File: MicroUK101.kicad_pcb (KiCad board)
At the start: 2 copper layers, 99.7 x 92.5 mm, 31 parts, among them CON1 BARREL_JACK, J1 DB9, P1 CONN_02X02, P2 CONN_01X04, P3 CONN_02X01, P4 CONN_02X01, SW1 SW_PUSH, SW2 Switch_DPST, U1 6502, U10 74LS00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

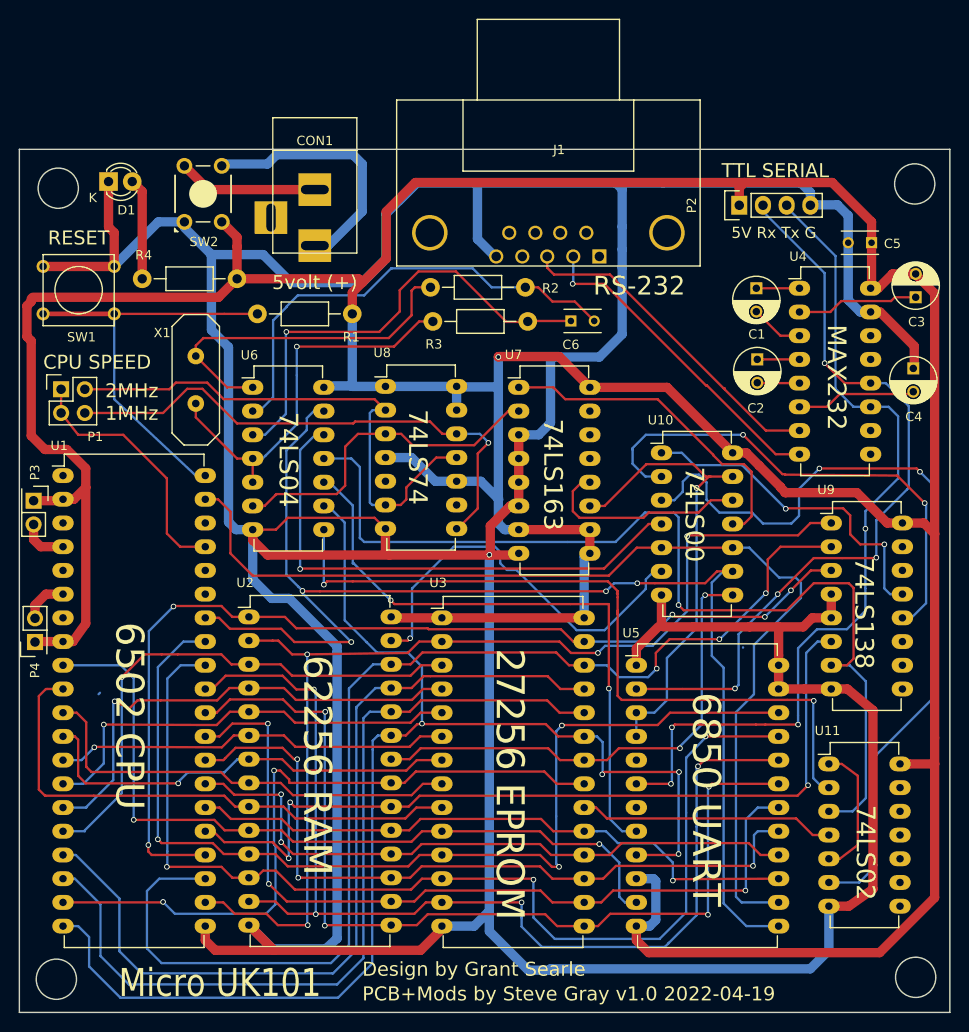
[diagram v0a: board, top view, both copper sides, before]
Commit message: Release 1.02
Fix Tx and Rx lines to RS-232. Ran DRC and fixed a bunch of small track
errors. Updated silkscreen, created new gerbers.
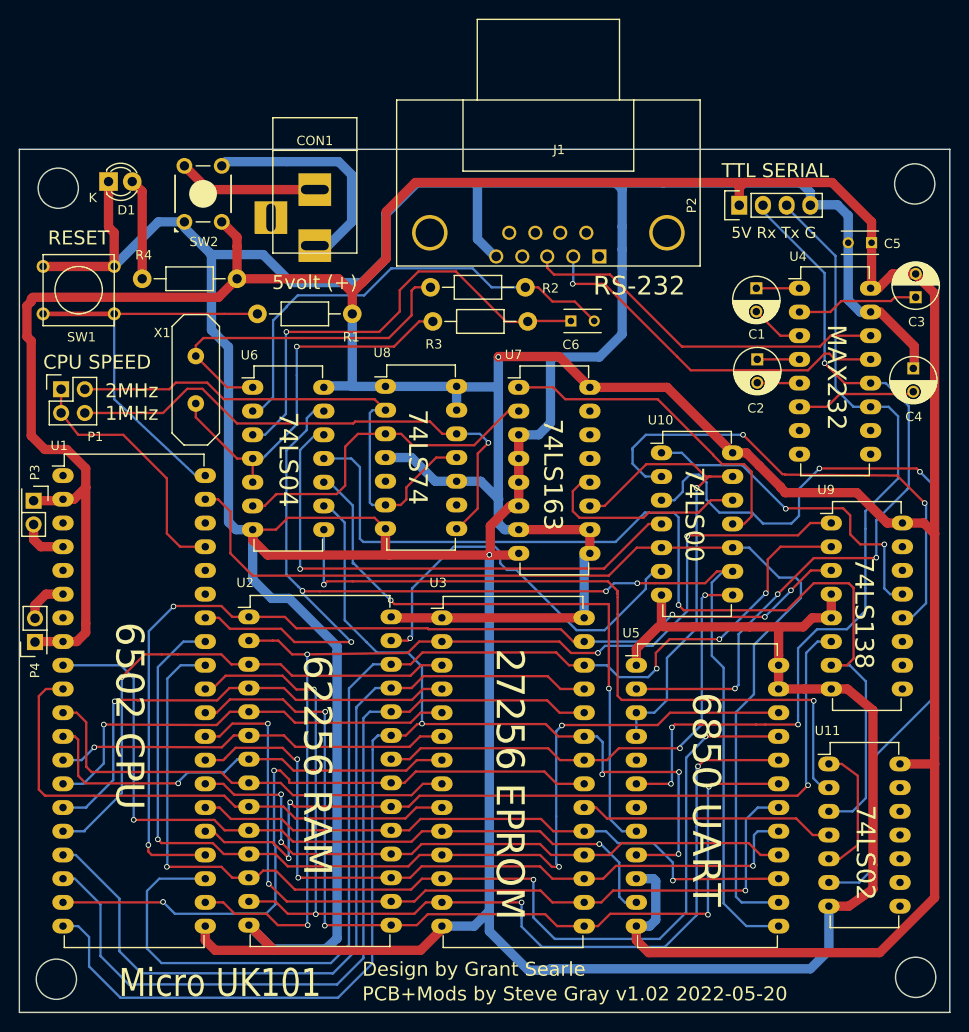
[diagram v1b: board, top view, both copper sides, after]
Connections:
- net R/~{W} renamed R/~{W}
- CON1 pad 3: Net-(CON1-Pad3) -> unconnected-(CON1-Pad3)
- J1 pad 1: Net-(J1-Pad1) -> unconnected-(J1-Pad1)
- J1 pad 4: Net-(J1-Pad4) -> unconnected-(J1-Pad4)
- J1 pad 6: Net-(J1-Pad6) -> unconnected-(J1-Pad6)
- J1 pad 7: Net-(J1-Pad7) -> unconnected-(J1-Pad7)
- J1 pad 8: Net-(J1-Pad8) -> unconnected-(J1-Pad8)
- J1 pad 9: Net-(J1-Pad9) -> unconnected-(J1-Pad9)
- U1 pad 3: Net-(U1-Pad3) -> unconnected-(U1-Pad3)
- U1 pad 35: Net-(U1-Pad35) -> unconnected-(U1-Pad35)
- U1 pad 36: Net-(U1-Pad36) -> unconnected-(U1-Pad36)
- U1 pad 38: Net-(U1-Pad38) -> unconnected-(U1-Pad38)
- U1 pad 5: Net-(U1-Pad5) -> unconnected-(U1-Pad5)
- U1 pad 7: Net-(U1-Pad7) -> unconnected-(U1-Pad7)
- U11 pad 10: Net-(U11-Pad10) -> unconnected-(U11-Pad10)
- U11 pad 11: Net-(U11-Pad11) -> unconnected-(U11-Pad11)
- U11 pad 12: Net-(U11-Pad12) -> unconnected-(U11-Pad12)
- U11 pad 13: Net-(U11-Pad13) -> unconnected-(U11-Pad13)
- U11 pad 8: Net-(U11-Pad8) -> unconnected-(U11-Pad8)
- U11 pad 9: Net-(U11-Pad9) -> unconnected-(U11-Pad9)
- U4 pad 10: Net-(U4-Pad10) -> unconnected-(U4-Pad10)
- U4 pad 13: Net-(U4-Pad13) -> Rx
- U4 pad 14: Net-(U4-Pad14) -> Tx
- U4 pad 7: Tx -> unconnected-(U4-Pad7)
- U4 pad 8: Rx -> unconnected-(U4-Pad8)
- U4 pad 9: Net-(U4-Pad9) -> unconnected-(U4-Pad9)
- U5 pad 5: Net-(U5-Pad5) -> unconnected-(U5-Pad5)
- U5 pad 7: Net-(U5-Pad7) -> unconnected-(U5-Pad7)
- U7 pad 13: Net-(U7-Pad13) -> unconnected-(U7-Pad13)
- U7 pad 14: Net-(U7-Pad14) -> unconnected-(U7-Pad14)
- U7 pad 15: Net-(U7-Pad15) -> unconnected-(U7-Pad15)
- U8 pad 5: Net-(U8-Pad5) -> unconnected-(U8-Pad5)
- U8 pad 9: Net-(U8-Pad9) -> unconnected-(U8-Pad9)
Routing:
- net Rx: track 34.8 -> 39.7 mm
- net Tx: track 35.5 -> 39.9 mm
- net Net-(CON1-Pad1): track 27.7 -> 24.7 mm
- net GND: track 530.4 -> 527.4 mm
- net 5V: track 462.4 -> 460.7 mm
- net Net-(U11-Pad2): track 81.5 -> 80.9 mm
- net TTL_Tx: vias 4 -> 3
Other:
- board text added: "PCB+Mods by Steve Gray v1.02 2022-05-20"
- board text removed: "PCB+Mods by Steve Gray v1.0 2022-04-19"
